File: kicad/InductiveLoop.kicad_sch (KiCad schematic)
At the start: 57 parts, among them U4 TLC555xD, U5 TLC555xD, U6 TLC555xD

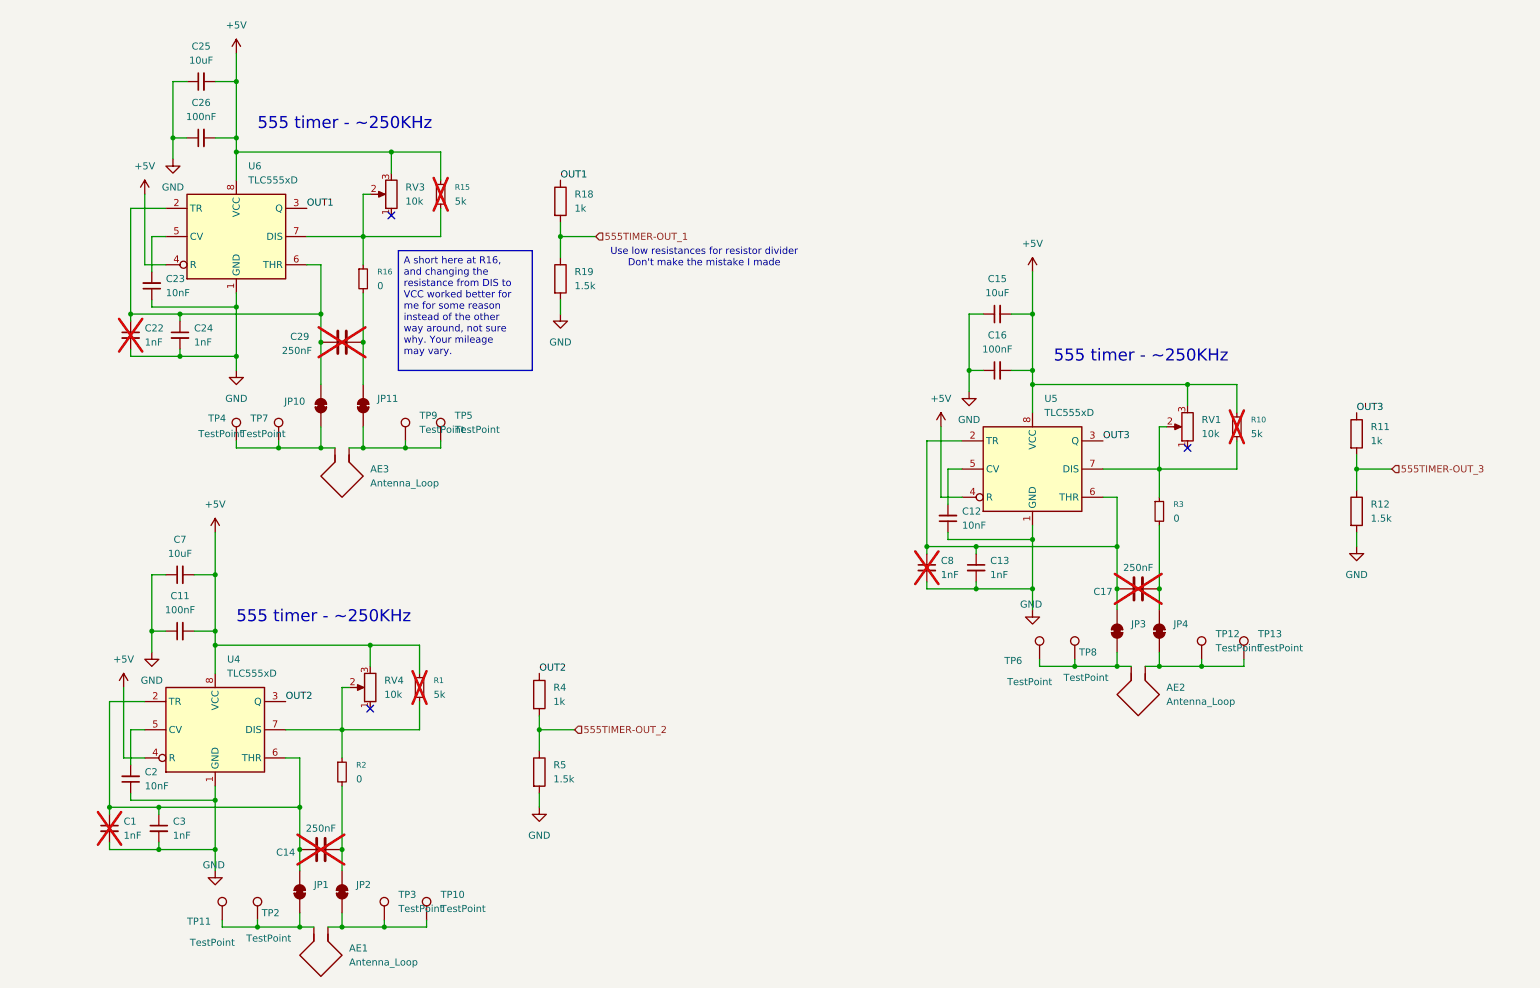
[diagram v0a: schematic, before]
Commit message: add comments to kicad schematic
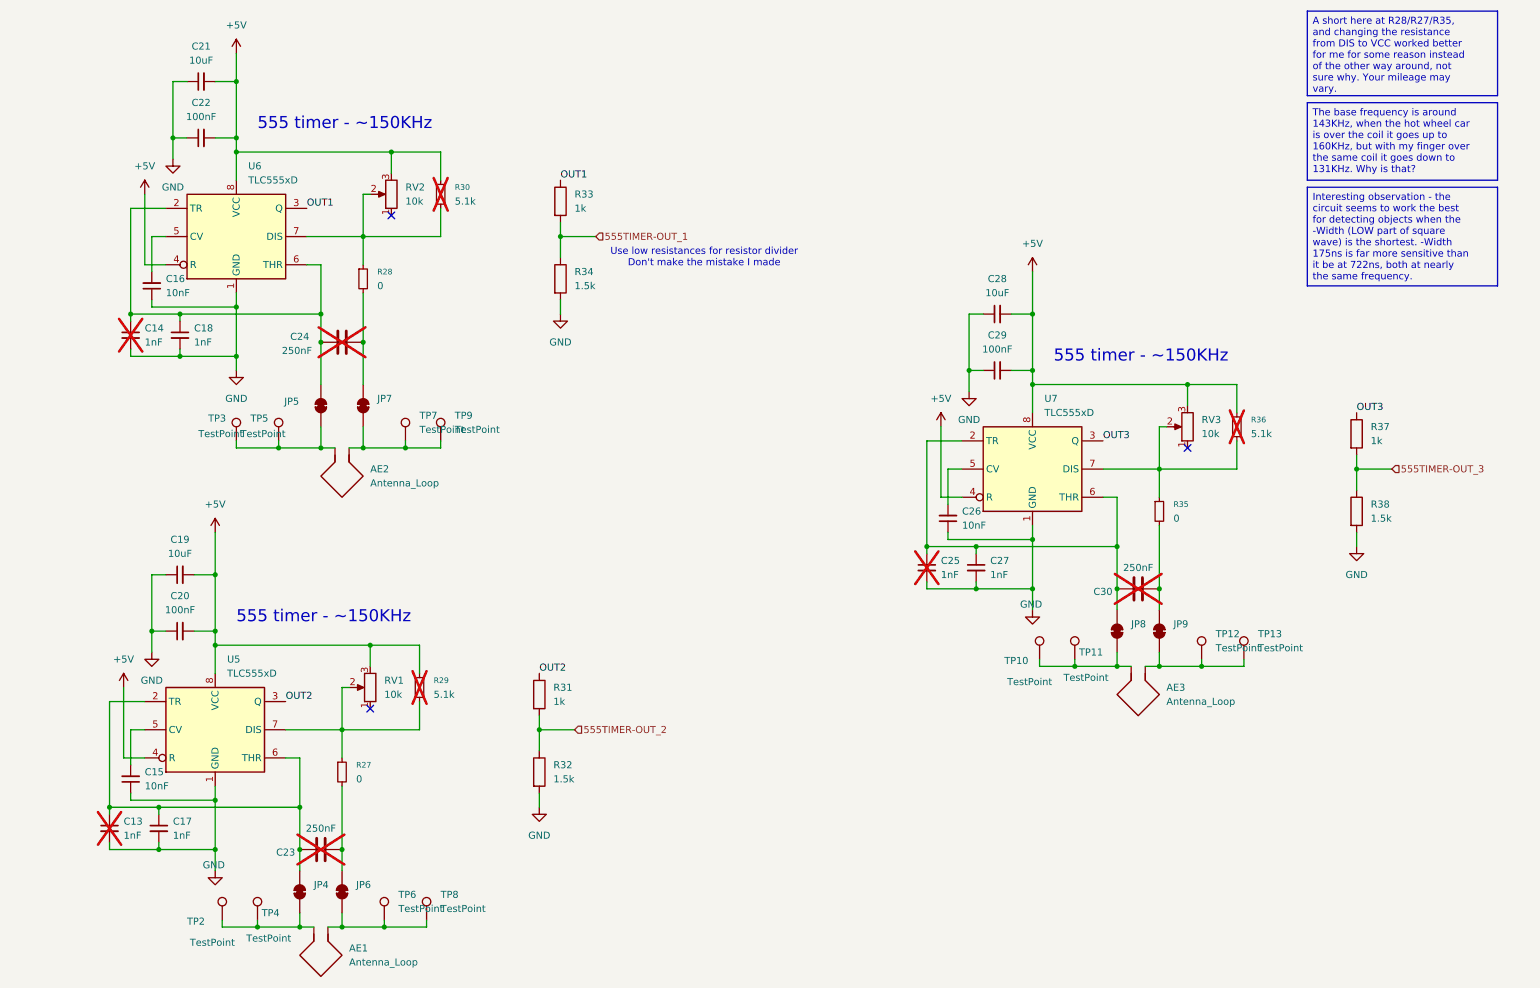
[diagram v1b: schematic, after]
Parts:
- R29: renamed from R1; value 5k -> 5.1k
- R30: renamed from R15; value 5k -> 5.1k
- R36: renamed from R10; value 5k -> 5.1k
- renumbered AE3 to AE2, AE2 to AE3, C1 to C13, C22 to C14, C2 to C15, C23 to C16, C3 to C17, C24 to C18, C7 to C19, C11 to C20, C25 to C21, C26 to C22, C14 to C23, C29 to C24, C8 to C25, C12 to C26, C13 to C27, C15 to C28, C16 to C29, C17 to C30, JP1 to JP4, JP10 to JP5, JP2 to JP6, JP11 to JP7, JP3 to JP8, JP4 to JP9, R2 to R27, R16 to R28, R4 to R31, R5 to R32, R18 to R33, R19 to R34, R3 to R35, R11 to R37, R12 to R38, RV4 to RV1, RV3 to RV2, RV1 to RV3, TP6 to TP10, TP8 to TP11, TP11 to TP2, TP4 to TP3, TP2 to TP4, TP7 to TP5, TP3 to TP6, TP9 to TP7, TP10 to TP8, TP5 to TP9, U4 to U5, U5 to U7
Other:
- note added: "555 timer - ~150KHz"
- note removed: "555 timer - ~250KHz"

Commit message: small pcb change
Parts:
- added JP1, JP2, JP3: SolderJumper_2_Open, Jumper:SolderJumper-2_P1.3mm_Open_RoundedPad1.0x1.5mm, symbol Jumper:SolderJumper_2_Open
- R29, R30, R36: now fitted
- U5, U6, U7: value TLC555xD -> TLC555CDR
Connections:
- net +5V renamed VBUS_{unregulated}
- net VBUS_{unregulated}: now also JP1.2 (B), JP2.2 (B), JP3.2 (B); no longer R29.1, R30.1, R36.1
- new net: JP1.1 (A), R30.1
- new net: JP2.1 (A), R29.1
- new net: JP3.1 (A), R36.1

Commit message: update!
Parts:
- added U8: 74LVC3G17V8-7, easyeda2kicad:VSSOP-8_L2.1-W2.4-P0.50-LS3.2-BL, symbol EASYEDA2KICAD:74LVC3G17V8-7
- R31, R32, R33, R34, R37, R38: now not fitted
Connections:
- net 555TIMER-OUT_1: now also U8.7 (1Y)
- net 555TIMER-OUT_2: now also U8.5 (2Y)
- net 555TIMER-OUT_3: now also U8.2 (3Y)
- net GND: now also U8.4 (GND)
- net OUT1: now also U8.1 (1A)
- net OUT2: now also U8.3 (2A)
- net OUT3: now also U8.6 (3A)
- net VBUS_{unregulated} renamed VBUS_SENSOR_IN
- new net +3.3V: U8.8 (VCC)
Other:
- note added: "Replaces resistor dividers"
- note added: "Use low resistances for resistor divider"
- note removed: "Use low resistances for resistor divider Don't make the mistake I made"

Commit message: more updates
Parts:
- renumbered C13 to C23, C14 to C24, C15 to C25, C16 to C26, C17 to C27, C18 to C28, C19 to C29, C20 to C30, C21 to C31, C22 to C32, C23 to C33, C24 to C34, C25 to C35, C26 to C36, C27 to C37, C28 to C38, C29 to C39, C30 to C40, JP4 to JP1, JP5 to JP2, JP6 to JP3, JP7 to JP4, JP2 to JP5, JP1 to JP6, JP8 to JP7, JP9 to JP8, JP3 to JP9, R27 to R35, R28 to R36, R29 to R37, R30 to R38, R31 to R39, R32 to R40, R33 to R41, R34 to R42, R35 to R43, R36 to R44, R37 to R45, R38 to R46, TP2 to TP11, TP3 to TP12, TP4 to TP13, TP5 to TP14, TP6 to TP15, TP7 to TP16, TP8 to TP17, TP9 to TP18, TP10 to TP19, TP11 to TP20, TP12 to TP21, TP13 to TP22, U5 to U6, U6 to U7, U7 to U9
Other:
- note added: "Buffer to Replaces resistor dividers"
- note removed: "Replaces resistor dividers"

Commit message: nothing
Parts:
- removed C23, C24, C35: 1nF, Capacitor_THT:C_Radial_D5.0mm_H11.0mm_P2.00mm, symbol Device:C_Small
- removed C33, C34, C40: 250nF, Capacitor_THT:C_Radial_D5.0mm_H11.0mm_P2.00mm, symbol Device:C
- RV1, RV2, RV3: now not fitted
- renumbered C36 to C33, C37 to C34, C38 to C35, C39 to C36, R35 to R40, R36 to R41, R37 to R42, R38 to R43, R39 to R44, R40 to R45, R41 to R46, R42 to R47, R43 to R48, R44 to R49, R45 to R50, R46 to R51, U9 to U10, U6 to U7, U7 to U8, U8 to U9
